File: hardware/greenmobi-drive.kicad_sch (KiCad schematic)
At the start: 17 parts, among them J1 USB_C_Receptacle_USB2.0_14P, J3 BAT, J4 CAN, J5 Sensors, U2 TJA1051T-3

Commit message: half bridges
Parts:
- removed J3: BAT, Connector_AMASS:AMASS_XT90PW-M_1x02_P10.90mm_Horizontal, symbol Connector_Generic_MountingPin:Conn_02x01_MountingPin
- removed J4: CAN, symbol Connector_Generic:Conn_01x02
- added D1: YELLOW, LED_SMD:LED_0805_2012Metric, symbol Device:LED
- added D2: RED, LED_SMD:LED_0805_2012Metric, symbol Device:LED
- added D3: GREEN, LED_SMD:LED_0805_2012Metric, symbol Device:LED
- added J2: GND, MountingHole:MountingHole_5.3mm_M5_DIN965_Pad, symbol Connector_Generic:Conn_01x01
- added J3: UBAT, MountingHole:MountingHole_5.3mm_M5_DIN965_Pad, symbol Connector_Generic:Conn_01x01
- added J5: CAN, Connector_JST:JST_GH_SM04B-GHS-TB_1x04-1MP_P1.25mm_Horizontal, symbol Connector_Generic:Conn_01x04
- added R10, R11, R9: 220, symbol Device:R
- added R3: 56k, Resistor_SMD:R_0402_1005Metric, symbol Device:R
- added R6: 2.2k, symbol Device:R
- C2: renamed from C16; footprint (none) -> Capacitor_SMD:C_0402_1005Metric
- C3: renamed from C15; footprint (none) -> Capacitor_SMD:C_0402_1005Metric
- renumbered C17 to C1, J5 to J1, J1 to J4, R16 to R1, R4 to R12, R3 to R13, R18 to R2, R15 to R4, R19 to R5, R20 to R7, R17 to R8, U2 to U1
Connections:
- net +3.3V: now also R9.1
- net +5V: now also J5.1 (Pin_1)
- net GND: now also D1.1 (K), D2.1 (K), D3.1 (K), J2.1 (Pin_1), J5.4 (Pin_4), R6.1
- net CAN_P: now reaches R14.1, U1.7 (CANH)
- net CAN_P: now also J5.2 (Pin_2)
- net CAN_N: now reaches R14.2, U1.6 (CANL)
- net CAN_N: now also J5.3 (Pin_3)
- new net: D2.2 (A), R10.2
- new net: D1.2 (A), R9.2
- new net: D3.2 (A), R11.2
- new net Regulators/BAT: J3.1 (Pin_1), R3.2
- new net mcu/LED_GREEN: R11.1
- new net mcu/LED_RED: R10.1
- new net mcu/Vin: R3.1, R6.2
- no-connect marks 4 -> 3
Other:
- added sheet Regulators (regulators.kicad_sch)
- added sheet half-bridge1 (half-bridge.kicad_sch)
- added sheet half-bridge2 (half-bridge.kicad_sch)
- sheet half-bridge ports: added Current_sense, HIGH, LOW, Phase_V_sense, TEMP, VS; removed none
- sheet mcu ports: added H1, H2, H3, I1, I2, I3, L1, L2, L3, LED_GREEN, LED_RED, T1, T2, T3, V1, V2, V3, Vin; removed none
- moved on the sheet: C1, C2, C3, J1, J4, R1, R12, R13, R14, R2, R4, R5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

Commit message: Placement study
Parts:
- added C21: 2.2u, symbol Device:C
- added R26: 5.1k, symbol Device:R
- added TH2: 10k, symbol Device:Thermistor_NTC
- J1: footprint (none) -> Connector_JST:JST_GH_SM06B-GHS-TB_1x06-1MP_P1.25mm_Horizontal
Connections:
- net +3.3V: now also R26.1
- net GND: now also C21.2, TH2.2
- new net MOS_TEMP: C21.1, R26.2, TH2.1
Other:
- sheet half-bridge ports: added Phase_V; removed Phase_V_sense, TEMP
- sheet half-bridge1 ports: added Phase_V; removed Phase_V_sense, TEMP
- sheet half-bridge2 ports: added Phase_V; removed Phase_V_sense, TEMP
- sheet mcu ports: added none; removed T3

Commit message: Power Layout
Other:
- company: (none) -> G-Pereira
- title: (none) -> GreenMobi Drive
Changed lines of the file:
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@@
 	(generator_version "9.0")
 	(paper "A4")
+	(title_block
+		(title "GreenMobi Drive")
+		(date "2025-07-02")
+		(rev "0.1")
+		(company "G-Pereira")
+	)
 	(junction
 		(at 86.36 34.29)
@@
 	)
 	(junction
+		(at 232.41 142.24)
+		(diameter 0)
+		(color 0 0 0 0)
+	)
+	(junction
 		(at 86.36 30.48)
 		(diameter 0)
@@
 	(junction
 		(at 203.2 85.09)
-		(diameter 0)
-		(color 0 0 0 0)
-	)
-	(junction
-		(at 232.41 142.24)
 		(diameter 0)
 		(color 0 0 0 0)
@@
 	(wire
 		(pts
+			(xy 232.41 142.24) (xy 236.22 142.24)
+		)
+		(stroke
+			(width 0)
+			(type default)
+		)
+	)
+	(wire
+		(pts
 			(xy 54.61 125.73) (xy 67.31 125.73)
 		)
@@
 	(wire
 		(pts
+			(xy 236.22 137.16) (xy 236.22 138.43)
+		)
+		(stroke
+			(width 0)
+			(type default)
+		)
+	)
+	(wire
+		(pts
 			(xy 113.03 88.9) (xy 133.35 88.9)
 		)
@@
 	(wire
 		(pts
-			(xy 232.41 138.43) (xy 236.22 138.43)
-		)
-		(stroke
-			(width 0)
-			(type default)
-		)
-	)
-	(wire
-		(pts
 			(xy 113.03 78.74) (xy 133.35 78.74)
 		)
@@
 	(wire
 		(pts
-			(xy 232.41 140.97) (xy 236.22 140.97)
-		)
-		(stroke
-			(width 0)
-			(type default)
-		)
-	)
-	(wire
-		(pts
 			(xy 158.75 33.02) (xy 158.75 34.29)
 		)
@@
 	(wire
 		(pts
+			(xy 236.22 142.24) (xy 236.22 140.97)
+		)
+		(stroke
+			(width 0)
+			(type default)
+		)
+	)
+	(wire
+		(pts
 			(xy 115.57 186.69) (xy 115.57 180.34)
 		)
@@
 	(wire
 		(pts
-			(xy 232.41 137.16) (xy 232.41 138.43)
-		)
-		(stroke
-			(width 0)
-			(type default)
-		)
-	)
-	(wire
-		(pts
-			(xy 232.41 140.97) (xy 232.41 142.24)
-		)
-		(stroke
-			(width 0)
-			(type default)
-		)
-	)
-	(wire
-		(pts
 			(xy 194.31 90.17) (xy 194.31 97.79)
 		)
@@
 	(wire
 		(pts
-			(xy 222.25 137.16) (xy 232.41 137.16)
-		)
-		(stroke
+			(xy 222.25 137.16) (xy 236.22 137.16)
+		)
+		(stroke

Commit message: Layout
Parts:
- removed D1: YELLOW, LED_SMD:LED_0805_2012Metric, symbol Device:LED
- removed D2: RED, LED_SMD:LED_0805_2012Metric, symbol Device:LED
- removed R10, R9: 220, symbol Device:R
- added D7: GREEN, LED_SMD:LED_1210_3225Metric, symbol Device:LED
- added D8: Red, LED_SMD:LED_1210_3225Metric, symbol Device:LED
- added Q2, Q3: MMBT3904, Package_TO_SOT_SMD:SOT-23, symbol Transistor_BJT:MMBT3904
- added R17: 15, Resistor_SMD:R_0603_1608Metric, symbol Device:R
- added R35: 68, Resistor_SMD:R_0603_1608Metric, symbol Device:R
- C1: footprint (none) -> Capacitor_SMD:C_0402_1005Metric
- D3: value GREEN -> Yellow; footprint LED_SMD:LED_0805_2012Metric -> LED_SMD:LED_1210_3225Metric; LCSC (none) -> C965826
- J1: symbol Connector_Generic:Conn_01x06 -> Connector_Generic_MountingPin:Conn_01x06_MountingPin
- J5: symbol Connector_Generic:Conn_01x04 -> Connector_Generic_MountingPin:Conn_01x04_MountingPin
- R1, R4, R8, TH2: footprint (none) -> Resistor_SMD:R_0402_1005Metric
- R11: value 220 -> 68; footprint (none) -> Resistor_SMD:R_0603_1608Metric
- R14: value 220 -> 120; footprint (none) -> Resistor_SMD:R_0402_1005Metric
- R3: footprint Resistor_SMD:R_0402_1005Metric -> Resistor_SMD:R_0805_2012Metric
- R6: footprint (none) -> Resistor_SMD:R_0805_2012Metric
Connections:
- net +3.3V: now also R11.1, R17.1, R35.1
- net GND: now also J1.MP (MountPin), J5.MP (MountPin), Q2.2 (E), Q3.2 (E)
- net mcu/LED_GREEN: now also Q2.1 (B); no longer R11.1
- net mcu/LED_RED: now also Q3.1 (B)
- new net: D7.1 (K), Q2.3 (C)
- new net: D7.2 (A), R17.2
- new net: D8.2 (A), R35.2
- new net: D8.1 (K), Q3.3 (C)
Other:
- moved on the sheet: D3, J2, R11

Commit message: Added IMU
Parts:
- added C39, C40: 100n, Capacitor_SMD:C_0402_1005Metric, symbol Device:C_Small
- added U11: BMI323, Package_LGA:Bosch_LGA-14_3x2.5mm_P0.5mm, symbol Sensor_Motion:BMI160
- C21: footprint (none) -> Capacitor_SMD:C_0402_1005Metric
- R2, R26, R5, R7: footprint (none) -> Resistor_SMD:R_0402_1005Metric
- R6: footprint Resistor_SMD:R_0805_2012Metric -> Resistor_SMD:R_0402_1005Metric
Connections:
- net +3.3V: now also C39.1, C40.1, U11.5 (VDDIO), U11.8 (VDD)
- net GND: now also C39.2, C40.2, U11.1 (SDO), U11.6 (GNDIO), U11.7 (GND)
- new net SCL: U11.13 (SCx)
- new net SDA: U11.14 (SDx)
- no-connect marks 3 -> 9
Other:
- moved on the sheet: C1, C2, C21, C3, D3, D7, D8, J1, J2, J3, J4, J5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

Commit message: Layout mostly done
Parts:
- D3: value Yellow -> Blue; LCSC C965826 -> (none)
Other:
- sheet mcu ports: added none; removed T1, T2
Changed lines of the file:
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@@
 	(wire
 		(pts
-			(xy 129.54 91.44) (xy 149.86 91.44)
-		)
-		(stroke
-			(width 0)
-			(type default)
-		)
-	)
-	(wire
-		(pts
 			(xy 209.55 114.3) (xy 176.53 114.3)
 		)
@@
 			)
 		)
-		(property "Datasheet" "https://www.bosch-sensortec.com/media/boschsensortec/downloads/datasheets/bst-bmi323-ds000.pdf"
+		(property "Datasheet" "https://www.bosch-sensortec.com/media/boschsensortec/downloads/datasheets/bst-bmi160-ds000.pdf"
 			(at 22.86 21.59 0)
 			(effects
@@
 			)
 		)
-		(property "Value" "Yellow"
+		(property "Value" "Blue"
 			(at 256.032 37.084 90)
 			(effects
@@
 			)
 		)
-		(property "LCSC" "C965826"
+		(property "LCSC" ""
 			(at 261.62 35.56 90)
 			(effects
@@
 			(effects
 				(font
-					(size 1.27 1.27)
-				)
-				(justify left)
-			)
-		)
-		(pin "T1" input
-			(at 149.86 91.44 180)
-			(effects
-				(font
-					(size 1.27 1.27)
-				)
-				(justify left)
-			)
-		)
-		(pin "T2" input
-			(at 149.86 115.57 180)
-			(effects
-				(font

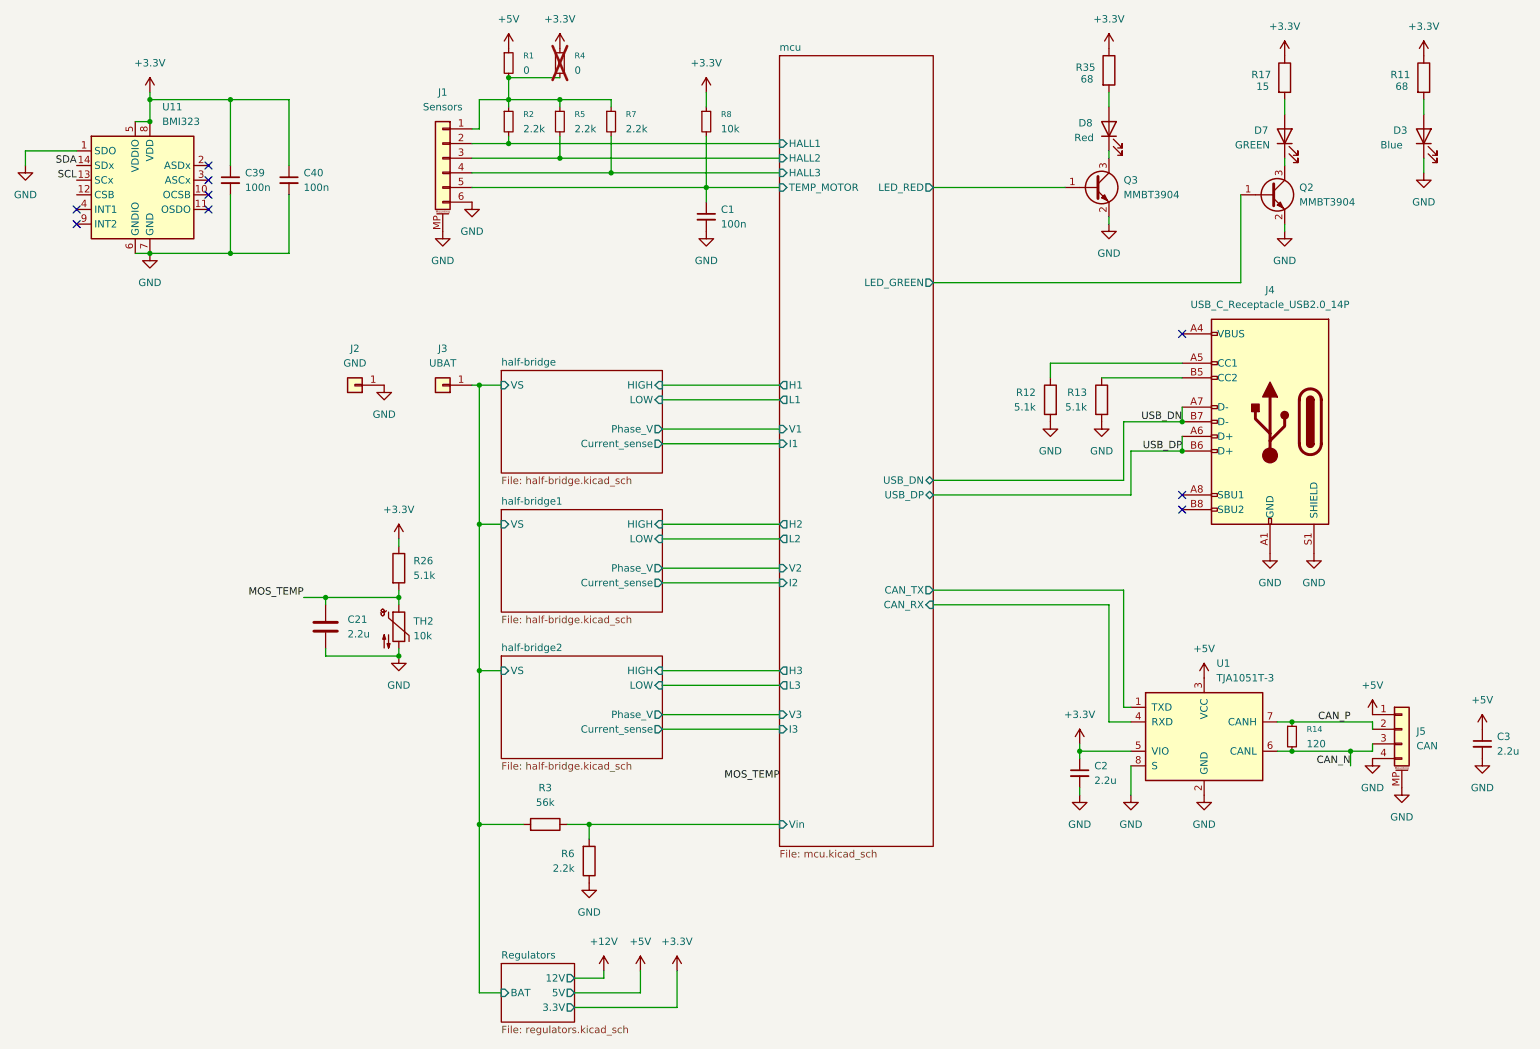
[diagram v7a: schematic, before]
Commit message: BOM optimizations
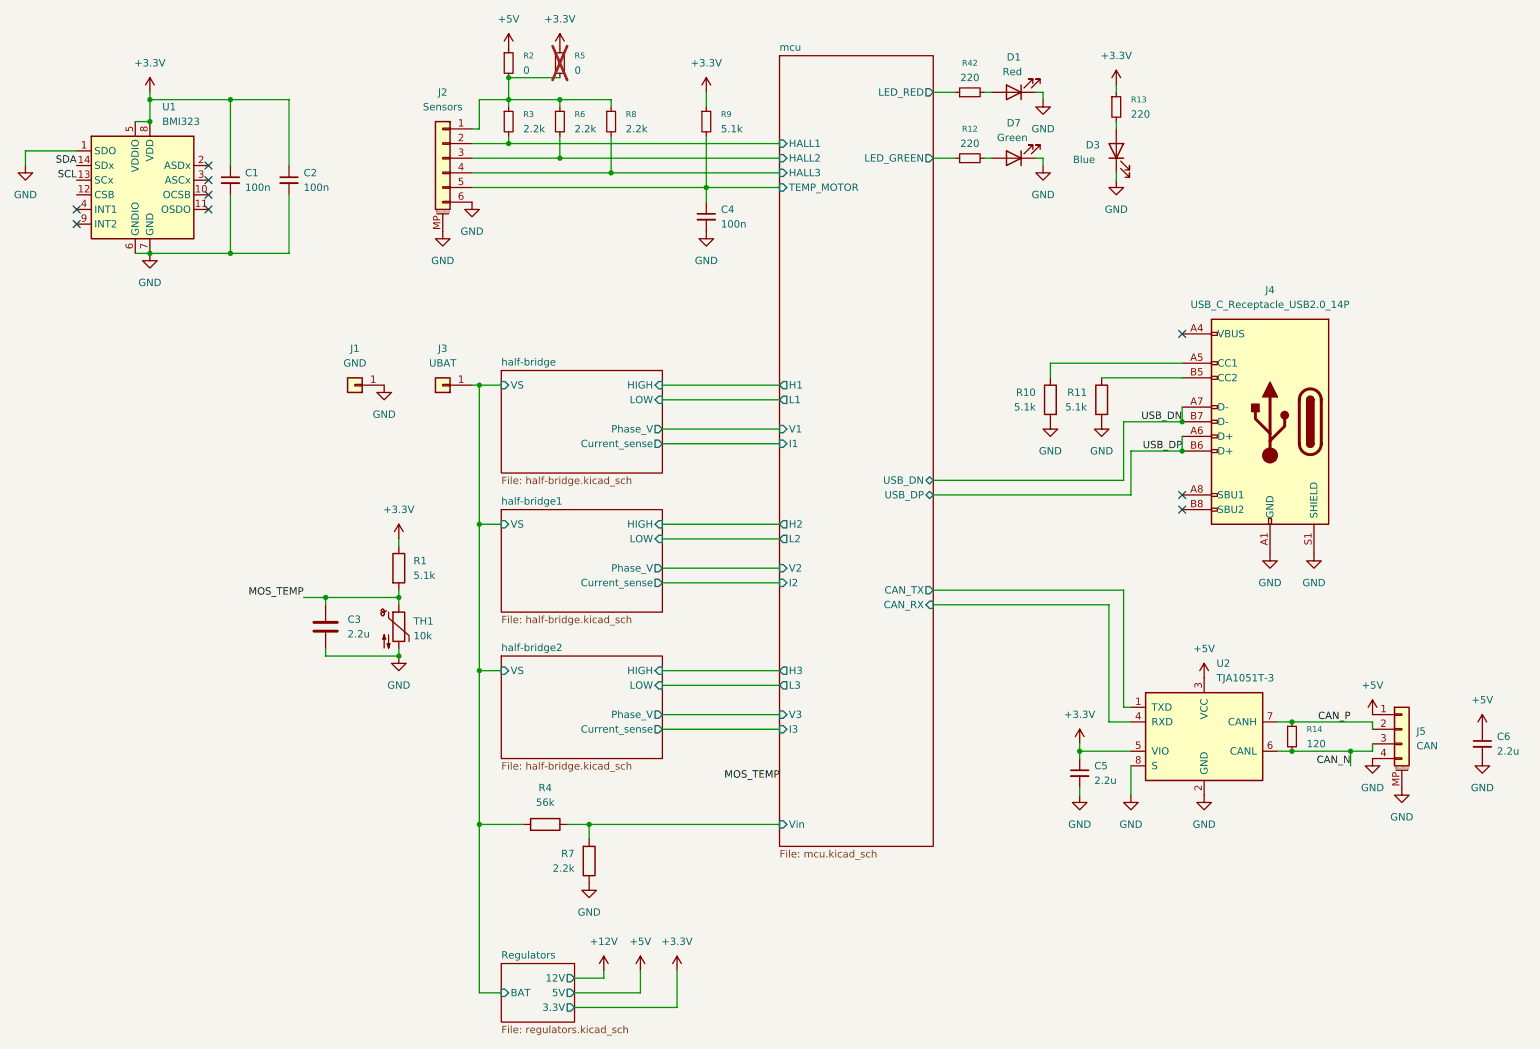
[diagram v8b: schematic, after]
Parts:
- removed Q2, Q3: MMBT3904, Package_TO_SOT_SMD:SOT-23, symbol Transistor_BJT:MMBT3904
- removed R11, R35: 68, Resistor_SMD:R_0603_1608Metric, symbol Device:R
- removed R17: 15, Resistor_SMD:R_0603_1608Metric, symbol Device:R
- added R12, R13, R42: 220, Resistor_SMD:R_0402_1005Metric, symbol Device:R_Small
- D1: renamed from D8; footprint LED_SMD:LED_1210_3225Metric -> LED_SMD:LED_0805_2012Metric; LCSC C965822 -> (none)
- D3: footprint LED_SMD:LED_1210_3225Metric -> LED_SMD:LED_0805_2012Metric
- D7: value GREEN -> Green; footprint LED_SMD:LED_1210_3225Metric -> LED_SMD:LED_0805_2012Metric; LCSC C965825 -> (none)
- R9: renamed from R8; value 10k -> 5.1k
- renumbered C39 to C1, C40 to C2, C21 to C3, C1 to C4, C2 to C5, C3 to C6, J2 to J1, J1 to J2, R26 to R1, R12 to R10, R13 to R11, R1 to R2, R2 to R3, R3 to R4, R4 to R5, R5 to R6, R6 to R7, R7 to R8, TH2 to TH1, U11 to U1, U1 to U2
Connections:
- net +3.3V: now also R13.1
- net GND: now also D1.1 (K), D7.1 (K)
- net mcu/LED_GREEN: now also R12.1
- net mcu/LED_RED: now also R42.1
- net at D7.2 (A): now also R12.2
- net at D1.2 (A): now also R42.2
- net at D3.2 (A): now also R13.2
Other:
- moved on the sheet: D1, D3
